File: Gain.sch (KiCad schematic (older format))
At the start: 73 parts, among them U5 AD8421, U6 OPA189, U7 OPA189

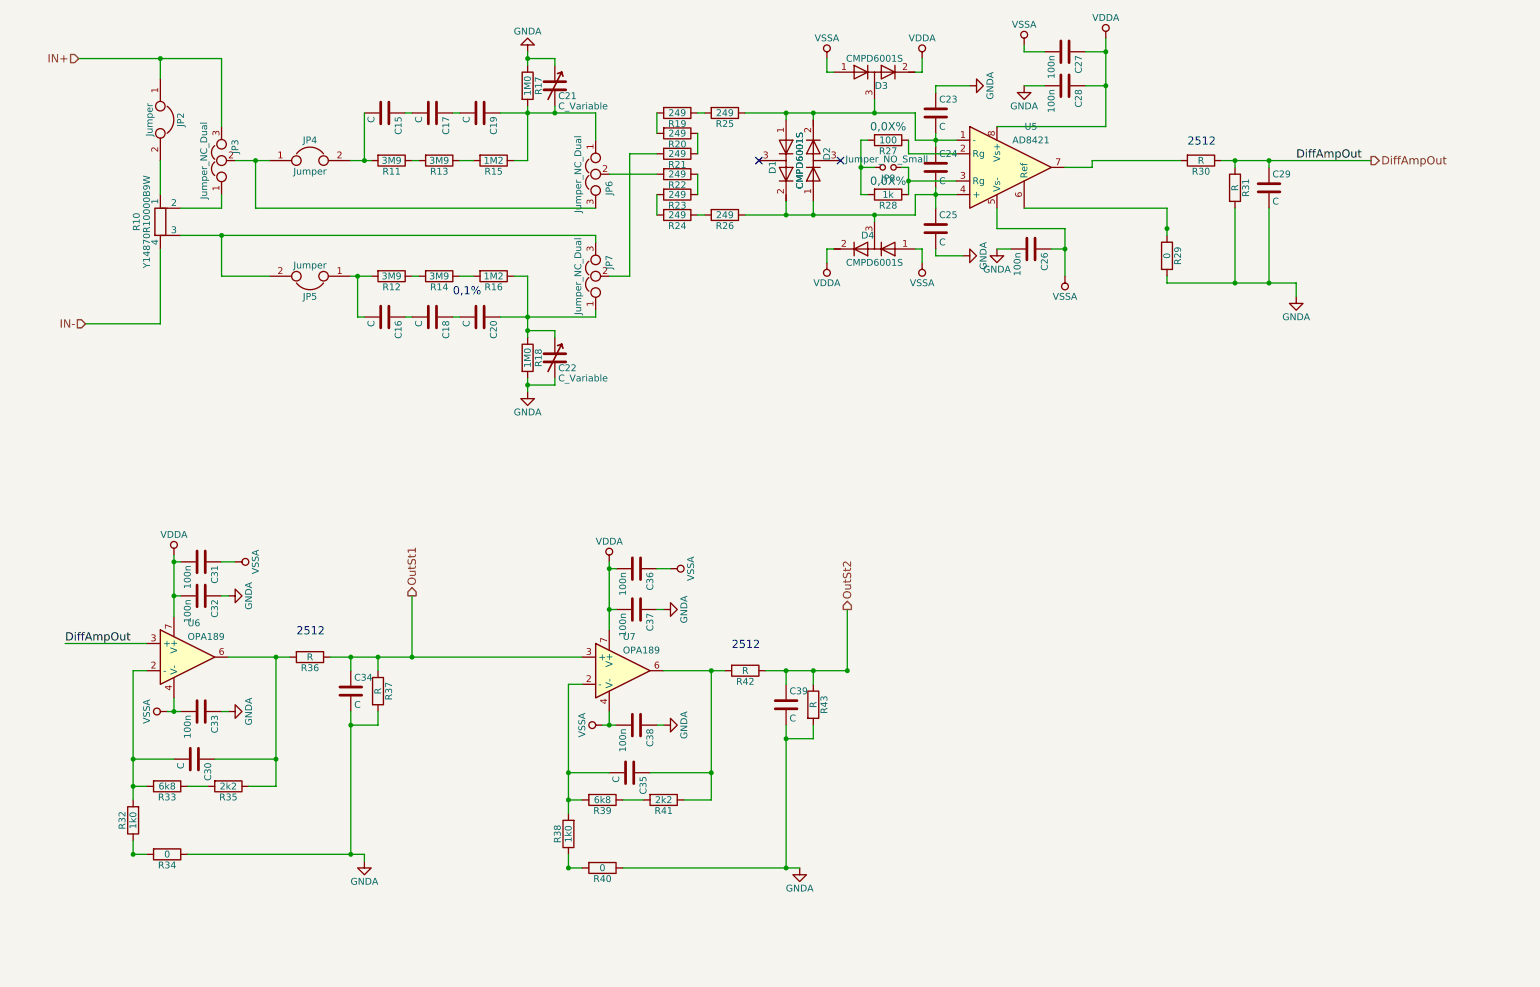
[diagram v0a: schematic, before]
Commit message: Schematic rearranged Added Netlist
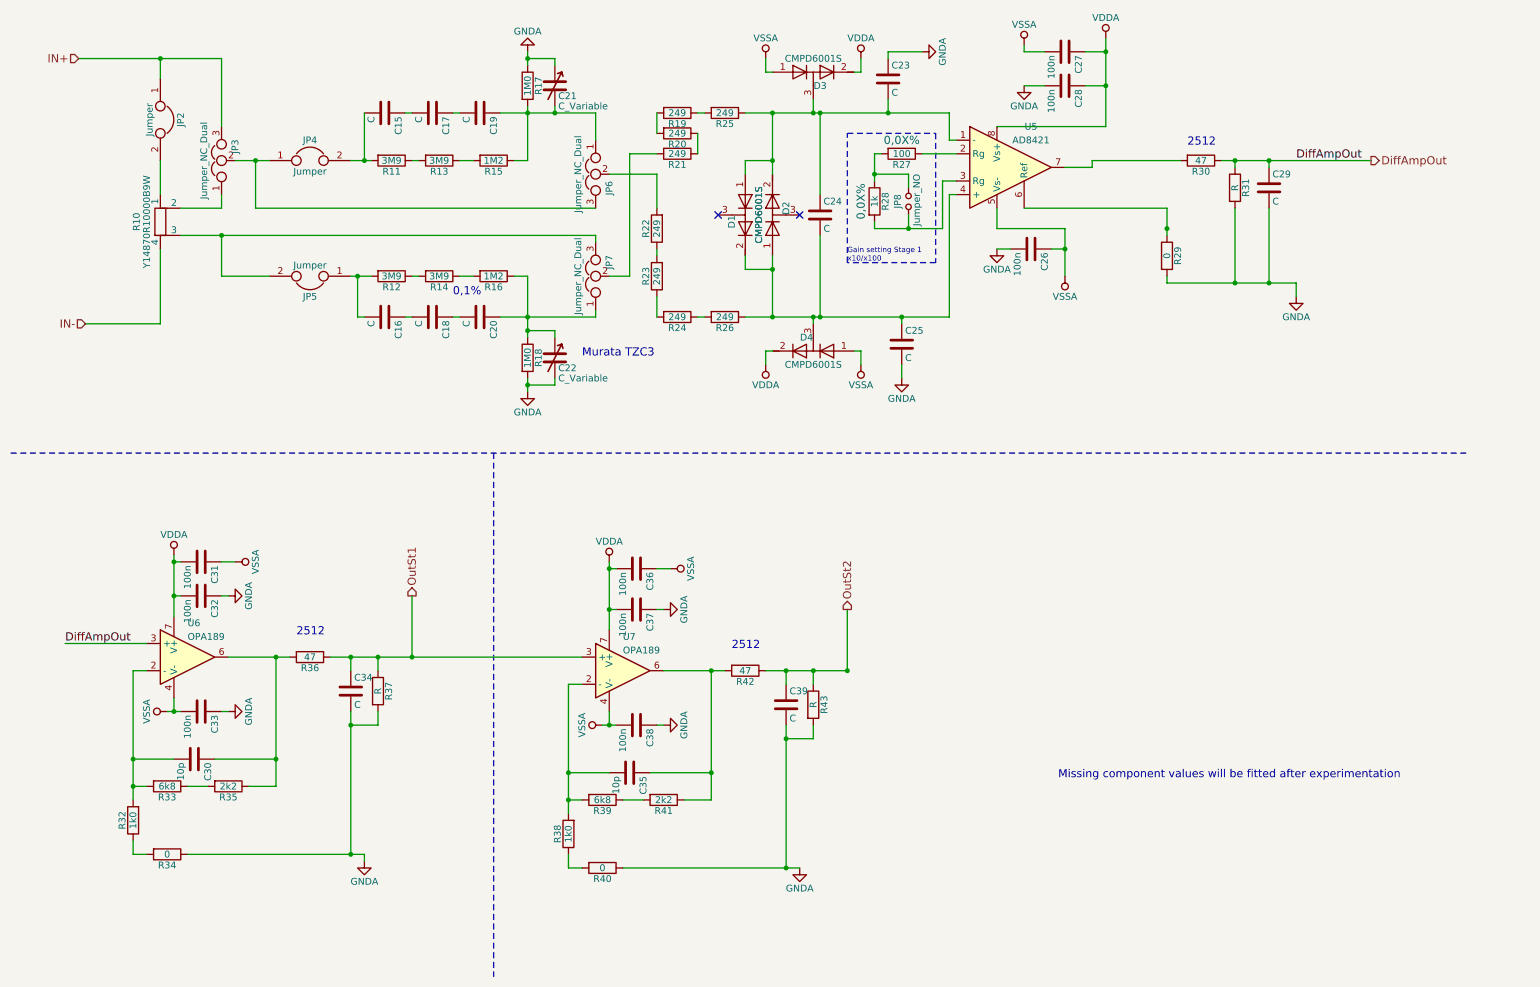
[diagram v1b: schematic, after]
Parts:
- C15, C16, C17, C18, C19, C20, C23, C24, C25, C26, C27, C28, C29, C31, C32, C33, C34, C36, C37, C38, C39: footprint (none) -> Capacitors_SMD:C_0805
- C21, C22: footprint (none) -> Capacitors_SMD:C_Trimmer_Murata_TZC3
- C30, C35: value C -> 10p; footprint (none) -> Capacitors_SMD:C_0805
- D1, D2, D3, D4: footprint (none) -> TO_SOT_Packages_SMD:SOT-23
- JP2, JP4, JP5: footprint (none) -> Pin_Headers:Pin_Header_Straight_1x02_Pitch2.54mm
- JP3, JP6, JP7: footprint (none) -> Pin_Headers:Pin_Header_Straight_1x03_Pitch2.54mm
- JP8: value Jumper_NO_Small -> Jumper_NO; footprint (none) -> Pin_Headers:Pin_Header_Straight_1x02_Pitch2.54mm
- R10: footprint (none) -> DiffAmp:CSM2512
- R11, R12, R13, R14, R15, R16, R17, R18, R19, R20, R21, R22, R23, R24, R25, R26, R27, R28, R29, R31, R32, R33, R34, R35, R37, R38, R39, R40, R41, R43: footprint (none) -> Resistors_SMD:R_0805
- R30, R36, R42: value R -> 47; footprint (none) -> Resistors_SMD:R_2512
- U5, U6, U7: footprint (none) -> Housings_SOIC:SOIC-8_3.9x4.9mm_Pitch1.27mm
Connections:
- net at JP8.1, U5.3 (Rg): now also R28.2; no longer R28.1
- net at JP8.2, R27.2: now also R28.1; no longer R28.2
- net at R24.2: now also R23.1; no longer R23.2
- net at R22.1: now also R23.2; no longer R23.1
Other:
- note added: "Gain setting Stage 1\nx10/x100"
- note added: "Missing component values will be fitted after experimentation"
- note added: "Murata TZC3"
- moved on the sheet: C23, C24, C25, D1, D2, D3, D4, JP8, R22, R23, R24, R26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

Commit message: Schematic pdf, Layout pdf + Gerber added
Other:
- note added: "Missing component values will be added later"
- note removed: "Missing component values will be fitted after experimentation"
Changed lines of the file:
@@
 Gain setting Stage 1\nx10/x100
 Text Notes 8200 6350 0    59   ~ 0
-Missing component values will be fitted after experimentation
+Missing component values will be added later
 Wire Notes Line
 	500  3950 11200 3950
